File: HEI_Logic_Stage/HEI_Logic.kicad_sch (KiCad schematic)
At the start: 38 parts, among them J5 Tag-Connect, SW1 SW_Push, U6 STM32F334C8T6, U7 LM4132-Q1 SOT-2

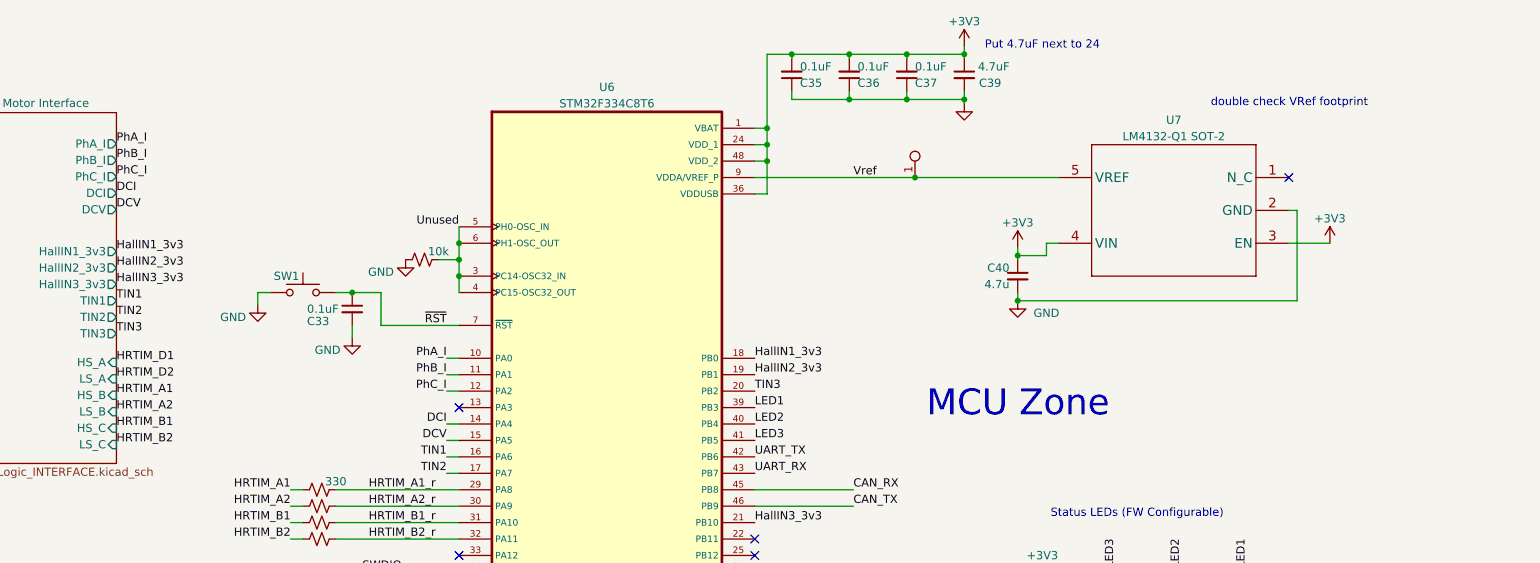
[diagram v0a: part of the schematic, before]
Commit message: almost completed new logic layout
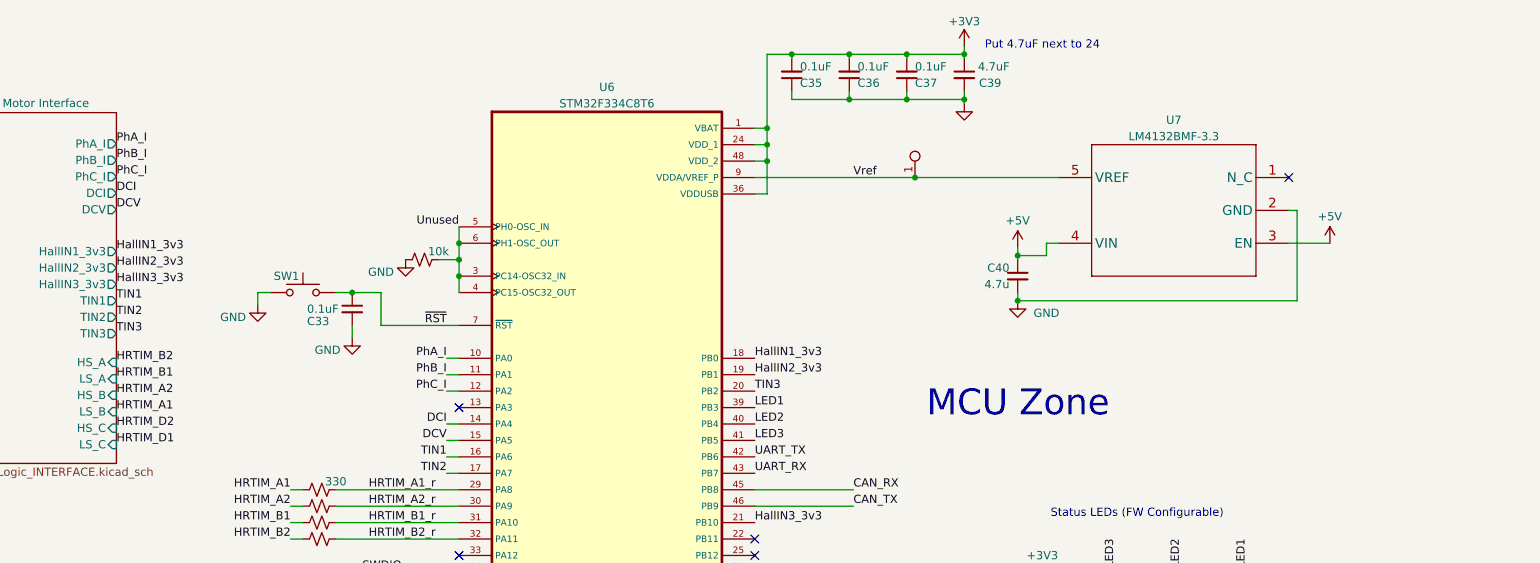
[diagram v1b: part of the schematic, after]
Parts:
- U7: value LM4132-Q1 SOT-2 -> LM4132BMF-3.3
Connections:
- net +3V3: no longer C40.1, U7.3 (EN), U7.4 (VIN)
- new net +5V: C40.1, U7.3 (EN), U7.4 (VIN)
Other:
- note removed: "double check VRef footprint"
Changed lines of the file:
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@@
 		)
 	)
-	(text "double check VRef footprint"
-		(exclude_from_sim no)
-		(at 255.27 29.845 0)
-		(effects
-			(font
-				(size 1.27 1.27)
-			)
-			(justify left bottom)
-		)
-	)
 	(text "FERRITES!\n"
 		(exclude_from_sim no)
@@
 		)
 	)
-	(label "HRTIM_A1"
+	(label "HRTIM_A2"
 		(at 86.106 74.295 0)
 		(fields_autoplaced yes)
@@
 		)
 	)
-	(label "HRTIM_B2"
+	(label "HRTIM_D1"
 		(at 86.106 81.915 0)
 		(fields_autoplaced yes)
@@
 		)
 	)
-	(label "HRTIM_B1"
+	(label "HRTIM_D2"
 		(at 86.106 79.375 0)
 		(fields_autoplaced yes)
@@
 		)
 	)
-	(label "HRTIM_A2"
+	(label "HRTIM_A1"
 		(at 86.106 76.835 0)
 		(fields_autoplaced yes)
@@
 		)
 	)
-	(label "HRTIM_D2"
+	(label "HRTIM_B1"
 		(at 86.106 71.755 0)
 		(fields_autoplaced yes)
@@
 		)
 	)
-	(label "HRTIM_D1"
+	(label "HRTIM_B2"
 		(at 86.106 69.215 0)
 		(fields_autoplaced yes)
@@
 			)
 		)
-		(property "Value" "+3V3"
-			(at 273.685 46.99 0)
+		(property "Value" "+5V"
+			(at 273.685 46.6669 0)
 			(effects
 				(font
@@
 			)
 		)
-		(property "Value" "LM4132-Q1 SOT-2"
+		(property "Value" "LM4132BMF-3.3"
 			(at 249.555 34.29 0)
 			(effects
@@
 			)
 		)
-		(property "Datasheet" "https://www.digikey.com/en/products/detail/texas-instruments/LM4132AQ1MFT3-0/5278911"
+		(property "Datasheet" "https://www.digikey.com/en/products/detail/texas-instruments/LM4132BMF-3-3-NOPB/1206359"
 			(at 249.555 57.15 0)
 			(effects
@@
 			)
 		)
-		(property "Value" "+3V3"
-			(at 225.425 47.625 0)
+		(property "Value" "+5V"
+			(at 225.425 47.3019 0)
 			(effects
 				(font

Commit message: main portion of logic drc done
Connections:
- net LED1: now also U6.26 (PB13); no longer U6.39 (PB3)
- net LED2: now also U6.25 (PB12); no longer U6.40 (PB4)
- net LED3: now also U6.22 (PB11); no longer U6.41 (PB5)
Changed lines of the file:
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@@
 	)
 	(no_connect
-		(at 184.785 96.52)
+		(at 184.785 81.28)
 	)
 	(no_connect
-		(at 184.785 101.6)
-	)
-	(no_connect
-		(at 184.785 99.06)
+		(at 184.785 78.74)
 	)
 	(no_connect
@@
 	(no_connect
 		(at 39.37 132.08)
+	)
+	(no_connect
+		(at 184.785 76.2)
 	)
 	(wire
@@
 		)
 	)
-	(label "LED2"
-		(at 184.785 78.74 0)
-		(fields_autoplaced yes)
-		(effects
-			(font
-				(size 1.27 1.27)
-			)
-			(justify left bottom)
-		)
-	)
 	(label "HRTIM_D1"
 		(at 213.36 104.14 0)
@@
 		)
 	)
+	(label "LED1"
+		(at 184.785 101.6 0)
+		(fields_autoplaced yes)
+		(effects
+			(font
+				(size 1.27 1.27)
+			)
+			(justify left bottom)
+		)
+	)
 	(label "PhB_I"
 		(at 137.16 71.12 180)
@@
 		)
 	)
+	(label "LED2"
+		(at 184.785 99.06 0)
+		(fields_autoplaced yes)
+		(effects
+			(font
+				(size 1.27 1.27)
+			)
+			(justify left bottom)
+		)
+	)
 	(label "CAN_TX"
 		(at 49.53 52.07 0)
@@
 		)
 	)
+	(label "LED3"
+		(at 184.785 96.52 0)
+		(fields_autoplaced yes)
+		(effects
+			(font
+				(size 1.27 1.27)
+			)
+			(justify left bottom)
+		)
+	)
 	(label "TIN1"
 		(at 137.16 83.82 180)
@@
 		)
 	)
-	(label "LED1"
-		(at 184.785 76.2 0)
-		(fields_autoplaced yes)
-		(effects
-			(font
-				(size 1.27 1.27)
-			)
-			(justify left bottom)
-		)
-	)
 	(label "Vref"
 		(at 59.69 45.72 180)
@@
 		(fields_autoplaced yes)
 		(effects
-			(font
-				(size 1.27 1.27)
-			)
-			(justify left bottom)
-		)
-	)
-	(label "LED3"
-		(at 184.785 81.28 0)
-		(fields_autoplaced yes)
-		(effects

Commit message: final tweaks to logic, silkscreen not done
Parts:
- removed SW1: SW_Push, GTSR_KiCAD_Footprints:KMR223GLFG, symbol Switch:SW_Push
- added SW1: KMR223GLFG, HEI_Logic:KMR223GLFG, symbol HEI_Logic:KMR223GLFG
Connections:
- net GND: now also SW1.2, SW1.G1
- net ~{RST}: now also SW1.4
- removed net Unused: R61.2, U6.3 (PC14-OSC32_IN), U6.4 (PC15-OSC32_OUT), U6.44 (PH3-BOOT0), U6.5 (PH0-OSC_IN), U6.6 (PH1-OSC_OUT)
- new net: R61.2, U6.44 (PH3-BOOT0)
- no-connect marks 10 -> 16

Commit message: schematic updates - logic
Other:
- note removed: "FERRITES!"
- note removed: "TODOs: - Consider 12->iso->5 for main power, then 5->12 for hall option? - Select 5V_MCU supply, check all power supply current budgets"
- moved on the sheet: C33, H2, J5, R71, R72, R73, R74, R75, R77, R78, R79, SW1
